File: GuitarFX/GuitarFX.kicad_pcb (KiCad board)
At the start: 4 copper layers, 70 x 85 mm, 122 parts, among them IC401 PCM3060PWR, J202 Screw_Terminal_01x02, J301 USB_C_Receptacle_USB2.0, J302 Conn_ARM_SWD_TagConnect_TC2030, J303 Screw_Terminal_01x06, J401 Screw_Terminal_01x02, J402 Screw_Terminal_01x02, SW301 SW_SPDT, U201 NCP718xSN500, U202 NCP1117-3.3_SOT223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

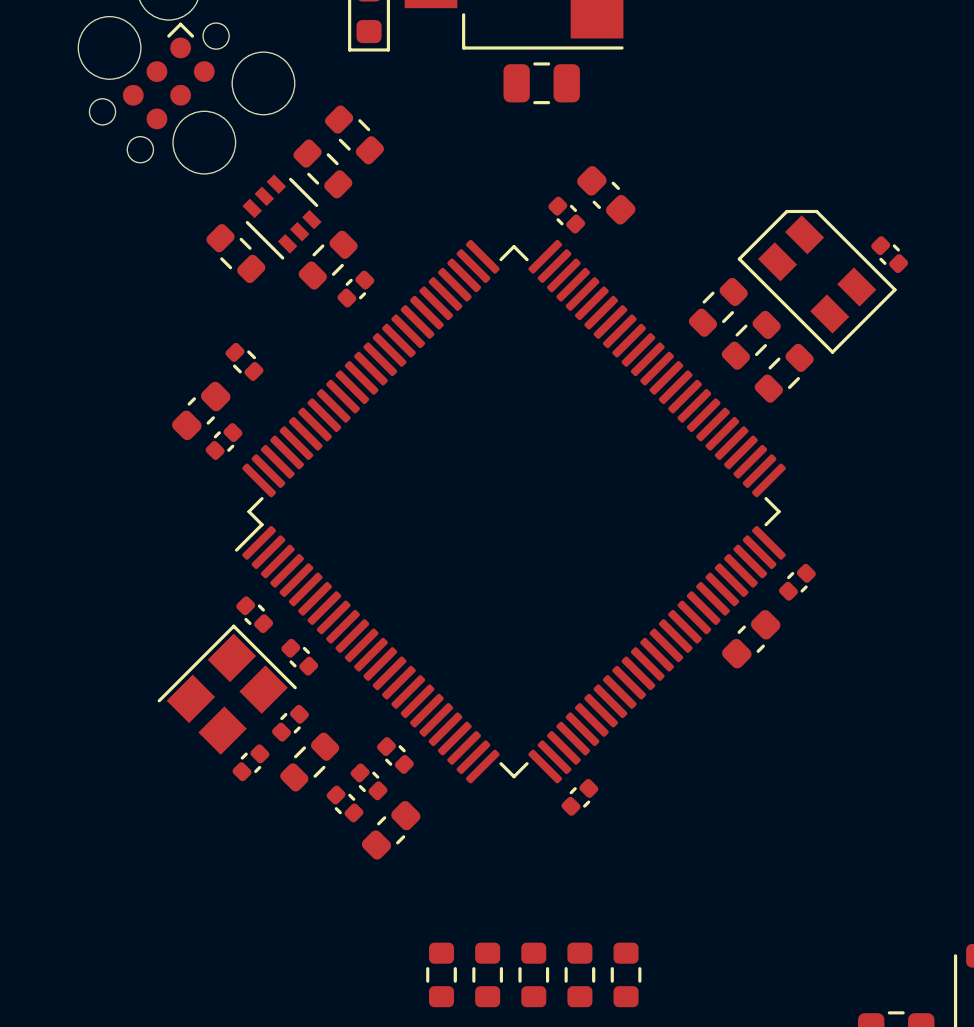
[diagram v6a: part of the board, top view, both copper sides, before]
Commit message: Routed mcu decoupling caps and crystal
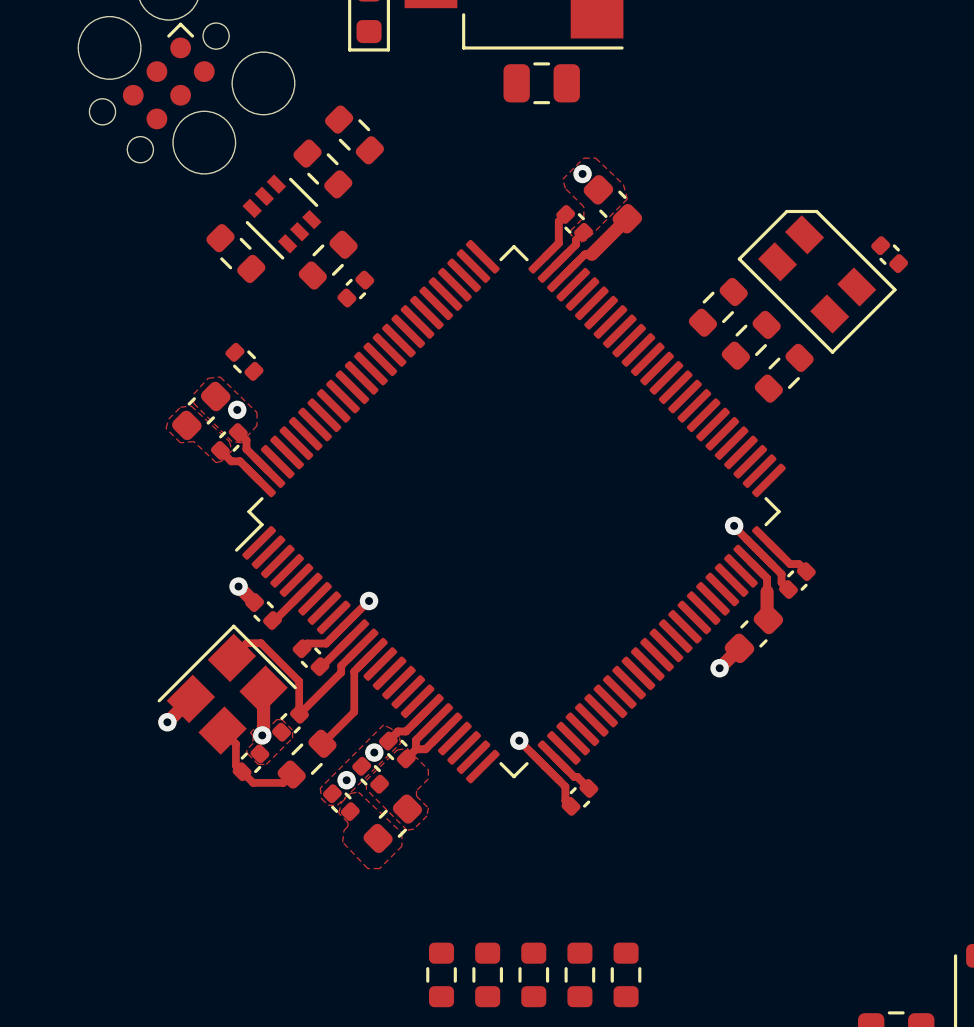
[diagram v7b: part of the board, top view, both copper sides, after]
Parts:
- moved C304 0.44 mm to (147.3, 78.0)
- moved C307 0.43 mm to (137.3, 94.5)
- moved C319 0.42 mm to (148.8, 77.2)
- moved C303 0.36 mm to (135.5, 92.7)
- moved C309 0.26 mm to (139.6, 98.9)
- moved FB301 0.26 mm to (140.4, 100.8)
- moved C318 0.23 mm to (154.1, 93.5)
- moved C308 0.22 mm to (140.6, 98.0)
- moved C302 0.20 mm to (134.2, 86.2)
- moved R302 0.15 mm to (137.2, 98.3)
- moved C310 0.15 mm to (138.4, 100.0)
- moved C306 0.06 mm to (155.8, 91.5)
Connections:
- J303 pad 5: VDDA -> +3.3V
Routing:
- net GND: track 0.00 -> 20.4 mm, vias 0 -> 11
- net +3.3V: track 0.00 -> 11.0 mm
- net /MCU/HSE_IN: track 0.00 -> 8.23 mm
- net /MCU/HSE_OUT: track 0.00 -> 4.14 mm
- net Net-(C315-Pad1): track 0.00 -> 4.06 mm
- net VDDA: track 0.00 -> 3.38 mm
- net /MCU/MCU_VCAP2: track 0.00 -> 3.30 mm
- net /MCU/MCU_VCAP1: track 0.00 -> 2.48 mm
- added copper zone on F.Cu, net +3.3V
- added copper zone on F.Cu, net GND
- added copper zone on F.Cu, net VDDA

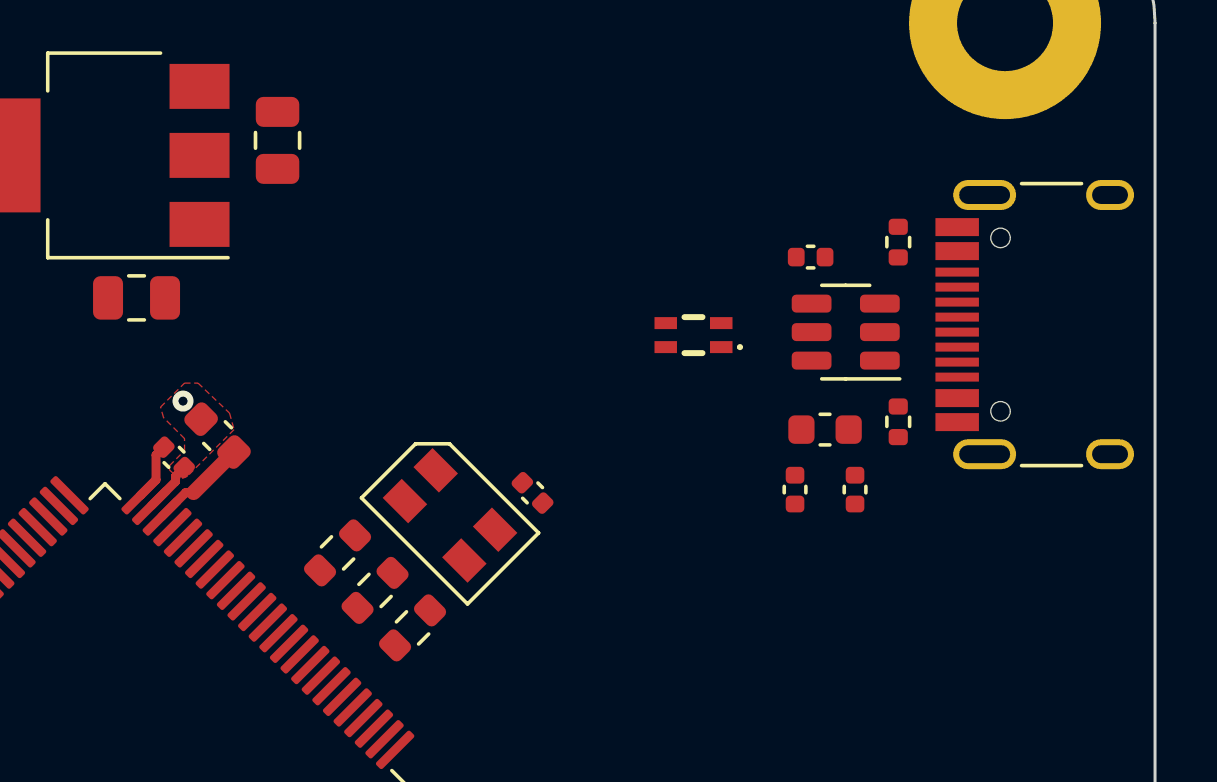
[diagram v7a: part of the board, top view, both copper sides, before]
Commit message: USB routing complete
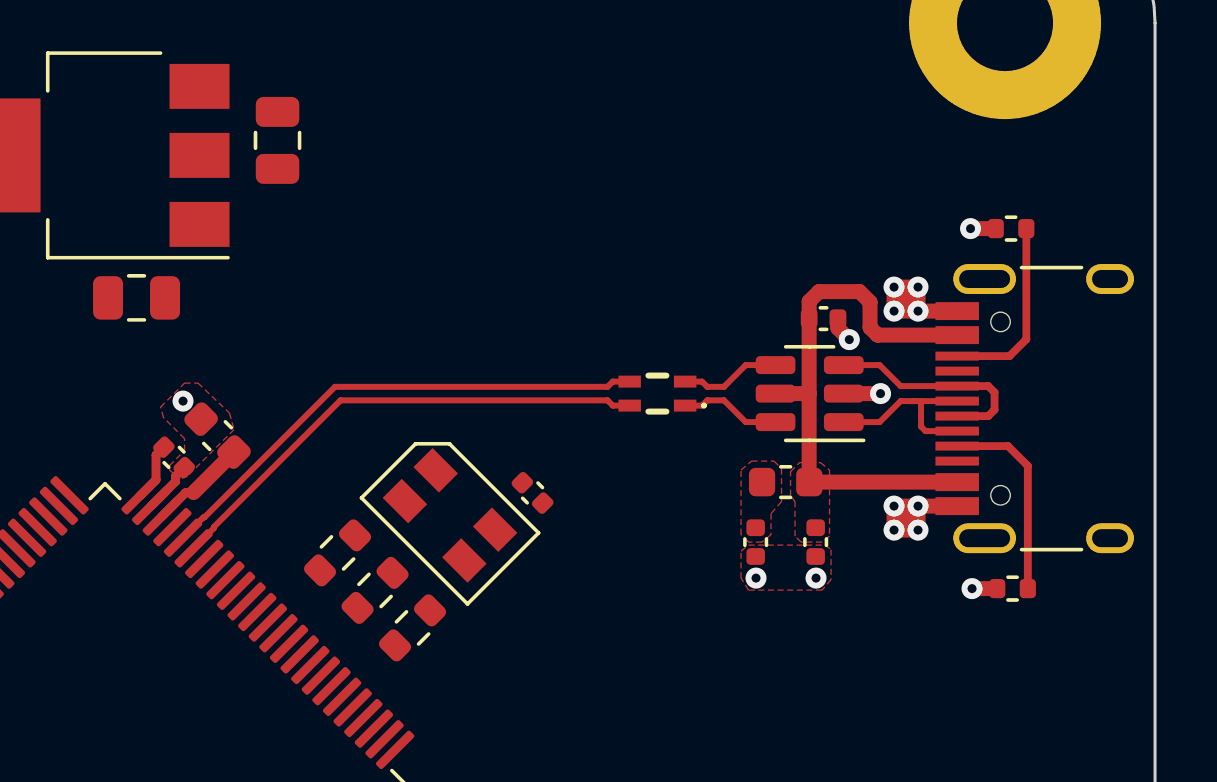
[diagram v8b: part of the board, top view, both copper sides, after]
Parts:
- moved R303 6.74 mm to (175.2, 82.3), turned to 180 degrees
- moved R304 3.79 mm to (175.2, 70.3), turned to 180 degrees
- moved J301 2.80 mm to (177.4, 76.3)
- moved U301 2.38 mm to (168.5, 75.8)
- moved FL301 2.29 mm to (163.4, 75.8)
- moved C311 2.19 mm to (168.7, 80.8)
- moved C312 2.19 mm to (166.7, 80.8)
- moved FB302 2.19 mm to (167.7, 78.8)
- moved C313 2.09 mm to (168.9, 73.3)
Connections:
- FL301 pad 3: /MCU/USB_FS_D- -> /MCU/USB_FS_D+
- FL301 pad 4: /MCU/USB_FS_D+ -> /MCU/USB_FS_D-
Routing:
- net VBUS: track 0.00 -> 18.2 mm
- net GND: track 20.4 -> 37.7 mm, vias 11 -> 25
- net /MCU/USB_FS_D+: track 0.00 -> 17.0 mm
- net /MCU/USB_FS_D-: track 0.00 -> 16.7 mm
- net /MCU/USB_CON_D+: track 0.00 -> 7.32 mm
- net /MCU/USB_CON_CC1: track 0.00 -> 6.72 mm
- net /MCU/USB_CON_CC2: track 0.00 -> 6.23 mm
- net /MCU/USB_CON_D-: track 0.00 -> 6.19 mm
- net /MCU/USB_CMC_D+: track 0.00 -> 3.39 mm
- net /MCU/USB_CMC_D-: track 0.00 -> 3.39 mm
- added copper zone on F.Cu, net VBUS
- added copper zone on F.Cu, net VUSB_FILT
